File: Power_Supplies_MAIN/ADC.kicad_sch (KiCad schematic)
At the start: 35 parts, among them IC1 PCM1865DBT, IC5 PCM1865DBT, J41 PINHD_1x1_Female, J42 PINHD_1x1_Female

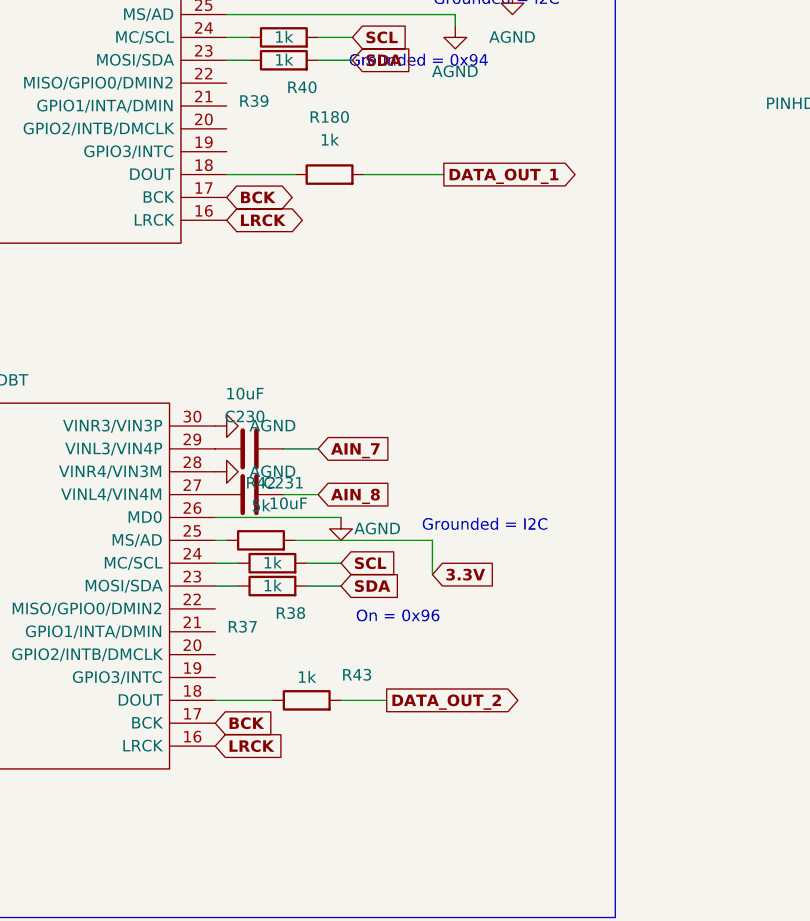
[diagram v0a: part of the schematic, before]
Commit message: updated main PCB to reflect changes w/ new mcu
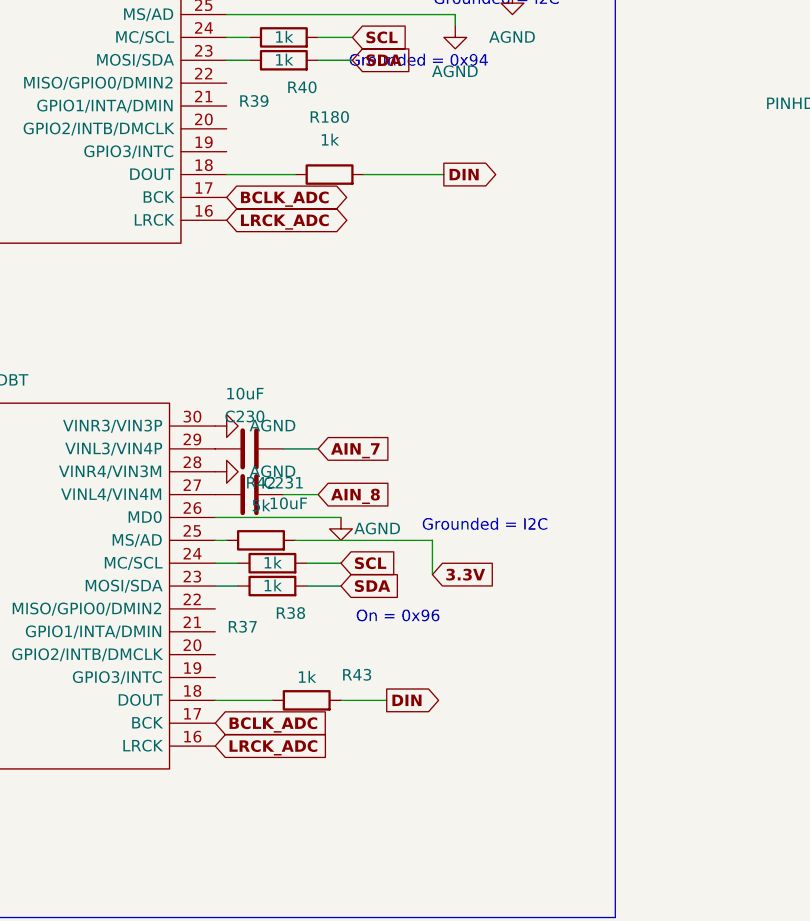
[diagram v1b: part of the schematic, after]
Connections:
- net DATA_OUT_1: no longer R180.2
- net DATA_OUT_2: no longer R43.2
- net BCK renamed BCLK_ADC
- net LRCK renamed LRCK_ADC
- new net DIN: R180.2, R43.2
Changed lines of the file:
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@@
 		)
 	)
-	(global_label "BCK"
+	(global_label "BCLK_ADC"
 		(shape bidirectional)
 		(at 119.38 80.01 0)
@@
 		)
 		(property "Intersheetrefs" "${INTERSHEET_REFS}"
-			(at 127.7625 80.01 0)
+			(at 133.3868 80.01 0)
 			(effects
 				(font
@@
 		)
 	)
-	(global_label "LRCK"
+	(global_label "LRCK_ADC"
 		(shape bidirectional)
 		(at 119.38 82.55 0)
@@
 		)
 		(property "Intersheetrefs" "${INTERSHEET_REFS}"
-			(at 128.7906 82.55 0)
+			(at 133.3868 82.55 0)
 			(effects
 				(font
@@
 		)
 	)
-	(global_label "LRCK"
+	(global_label "LRCK_ADC"
 		(shape input)
 		(at 118.11 140.97 0)
@@
 		)
 		(property "Intersheetrefs" "${INTERSHEET_REFS}"
-			(at 126.4093 140.97 0)
+			(at 131.0055 140.97 0)
 			(effects
 				(font
@@
 		)
 	)
-	(global_label "DATA_OUT_1"
+	(global_label "DIN"
 		(shape output)
 		(at 143.51 77.47 0)
@@
 		)
 		(property "Intersheetrefs" "${INTERSHEET_REFS}"
-			(at 158.1593 77.47 0)
+			(at 150.1765 77.47 0)
 			(effects
 				(font
@@
 		)
 	)
-	(global_label "BCK"
+	(global_label "BCLK_ADC"
 		(shape input)
 		(at 118.11 138.43 0)
@@
 		)
 		(property "Intersheetrefs" "${INTERSHEET_REFS}"
-			(at 125.3812 138.43 0)
+			(at 131.0055 138.43 0)
 			(effects
 				(font
@@
 		)
 	)
-	(global_label "DATA_OUT_2"
+	(global_label "DIN"
 		(shape output)
 		(at 137.16 135.89 0)
@@
 		)
 		(property "Intersheetrefs" "${INTERSHEET_REFS}"
-			(at 151.8093 135.89 0)
-			(effects
-				(font
+			(at 143.8265 135.89 0)
+			(effects
+				(font

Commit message: added changes that weeks wanted 🐷
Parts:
- removed C11, C12, C13, C220: 10uF, Capacitor_SMD:C_0805_2012Metric, symbol Device:C
- added R4, R5: 1k, Resistor_SMD:R_0805_2012Metric_Pad1.20x1.40mm_HandSolder, symbol Device:R
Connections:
- net 3.3V: now also C14.2, C16.2, C222.2, C224.2, IC1.8 (AVDD), IC5.8 (AVDD)
- net 3.3V_2: now also C15.1, C17.1, C223.1, C225.1, IC1.13 (DVDD), IC1.14 (IOVDD), IC5.13 (DVDD), IC5.14 (IOVDD)
- net MCLK: now also R4.1, R5.1; no longer IC1.15 (SCKI)
- net at IC5.15 (SCKI): now also R5.2
- new net: IC1.15 (SCKI), R4.2

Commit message: fixed a lot of stuff
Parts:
- removed C230, C231, C27, C28: 10uF, Capacitor_SMD:C_0805_2012Metric, symbol Device:C
- removed R180: 1k, Resistor_SMD:R_0805_2012Metric_Pad1.20x1.40mm_HandSolder, symbol Device:R
- removed R42: 5k, Resistor_SMD:R_0603_1608Metric_Pad0.98x0.95mm_HandSolder, symbol Device:R
- added C1, C2, C3, C4: 10uF, Capacitor_SMD:C_0805_2012Metric, symbol Device:C
- added D1, D2, D3, D4: LED, LED_SMD:LED_0402_1005Metric_Pad0.77x0.64mm_HandSolder, symbol PCM_SL_Devices:LED
- added R10, R6, R7: 2.2k, Resistor_SMD:R_0805_2012Metric, symbol Device:R
- added R34, R35, R73, R98: 0R, Resistor_SMD:R_0805_2012Metric_Pad1.20x1.40mm_HandSolder, symbol Device:R
- added R72: 2.2k, Resistor_SMD:R_0805_2012Metric_Pad1.20x1.40mm_HandSolder, symbol Device:R
- added R90, R91, R92, R93, R94, R95, R96, R97: 100k, PCM_Resistor_SMD_AKL:R_0402_1005Metric, symbol PCM_Resistor_AKL:R_0402
- R37, R38, R39, R40: value 1k -> 0R
- R4: value 1k -> 0
- R43: value 1k -> 2.2k
- R5: value 1k -> 2.2k; footprint Resistor_SMD:R_0805_2012Metric_Pad1.20x1.40mm_HandSolder -> Resistor_SMD:R_0805_2012Metric
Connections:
- net 3.3V: now also R34.1, R73.1, R98.2; no longer C14.2, C16.2, C222.2, C224.2, IC1.8 (AVDD), IC5.8 (AVDD)
- net 3.3V_2: now also R43.2, D2.2, D3.2, R72.2
- net AGND: now also R10.2, R6.2, R90.2, R91.2, R92.2, R93.2, R94.2, R95.2, R96.1, R97.1; no longer IC1.2 (VINR2/VIN2M), IC1.28 (VINR4/VIN3M), IC1.30 (VINR3/VIN3P), IC1.4 (VINR1/VIN2P), IC5.2 (VINR2/VIN2M), IC5.28 (VINR4/VIN3M), IC5.30 (VINR3/VIN3P), IC5.4 (VINR1/VIN2P)
- net AIN_1: now also R93.1
- net AIN_2: now also R92.1
- net AIN_3: now also C1.2, R90.1
- net AIN_4: now also C2.2, R91.1
- net AIN_5: now also R97.2
- net AIN_6: now also R94.1
- net AIN_7: now also C3.2, R95.1
- net AIN_8: now also C4.2, R96.2
- net DGND: now also R5.2, R7.2
- net DIN: now also IC1.18 (DOUT), IC5.18 (DOUT); no longer R43.2
- net MCLK: now also R35.1; no longer R5.1
- net SCL: now also R43.1
- net SDA: now also R72.1
- net at IC5.15 (SCKI): now also R35.2; no longer R5.2
- net at C19.2: now also IC1.4 (VINR1/VIN2P); no longer IC1.1 (VINL2/VIN1M)
- net at IC5.1 (VINL2/VIN1M): now also C3.1; no longer C226.2
- net at IC5.25 (MS/AD): now also R98.1
- new net: C14.2, C16.2, D4.2, IC1.8 (AVDD), R34.2
- new net: D2.1, R7.1
- new net: C2.1, IC1.2 (VINR2/VIN2M)
- new net: D1.1, R6.1
- new net: C222.2, C224.2, D1.2, IC5.8 (AVDD), R73.2
- new net: C4.1, IC5.2 (VINR2/VIN2M)
- new net: C226.2, IC5.4 (VINR1/VIN2P)
- new net: C1.1, IC1.1 (VINL2/VIN1M)
- new net: D3.1, R5.1
- new net: D4.1, R10.1
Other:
- moved on the sheet: C19, C226
